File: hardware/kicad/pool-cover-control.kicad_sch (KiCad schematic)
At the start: 20 parts, among them J1 DG128-5.08-04P, Q1 DMP4015SK3Q-13, U1 STM32G031K8Tx, U2 ULN2003A, U3 LMR14206, U4 PC817

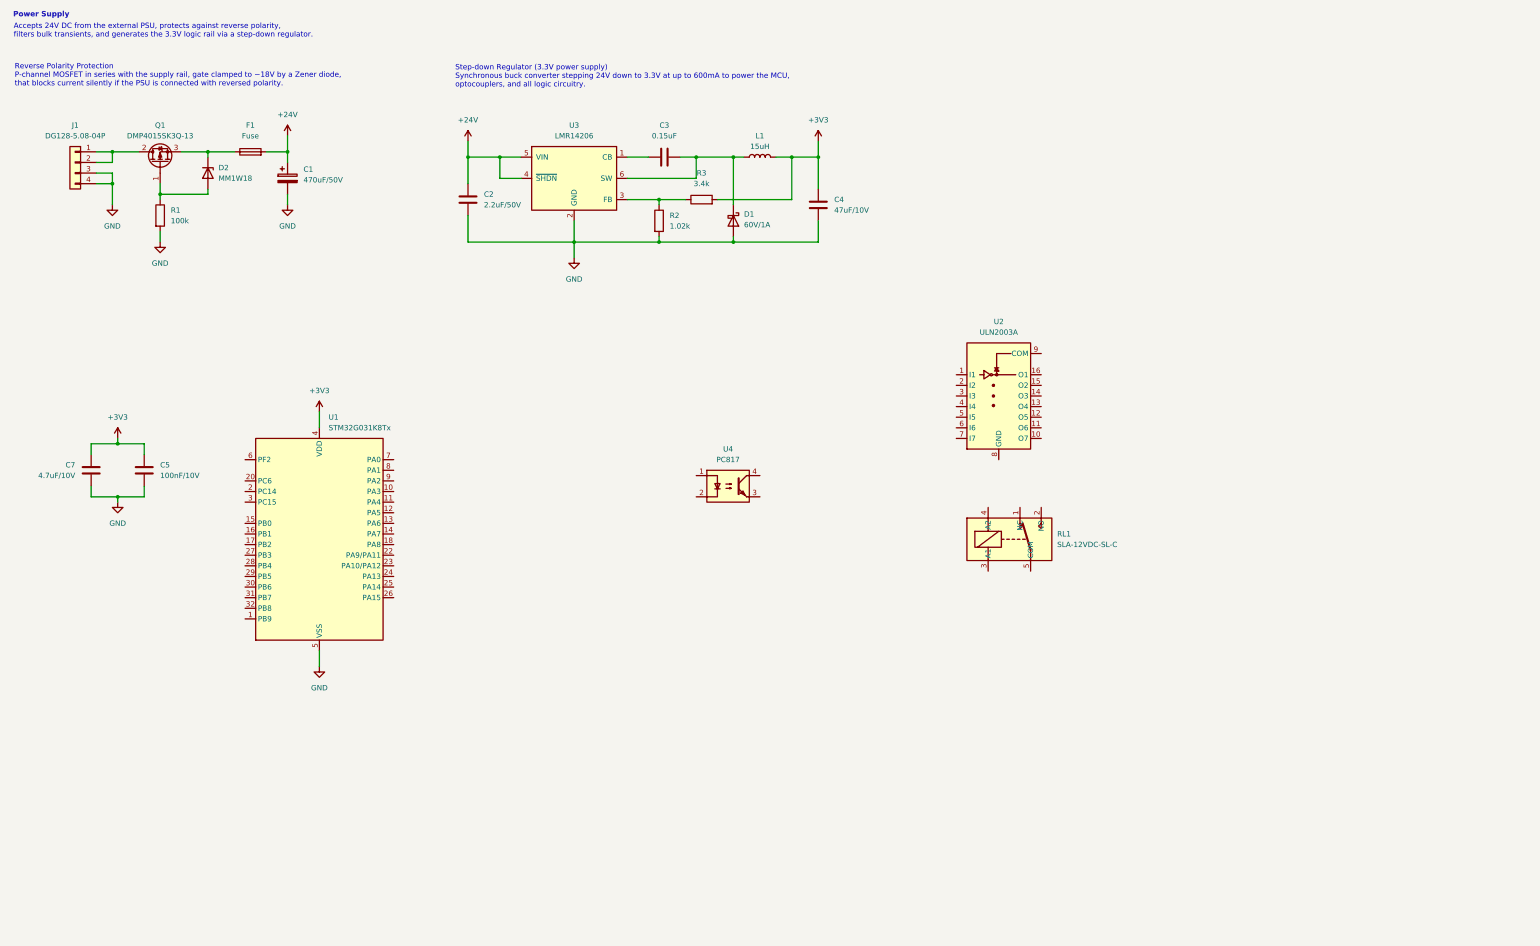
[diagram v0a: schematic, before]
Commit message: feat(hardware): implement SC2 H-bridge schematic
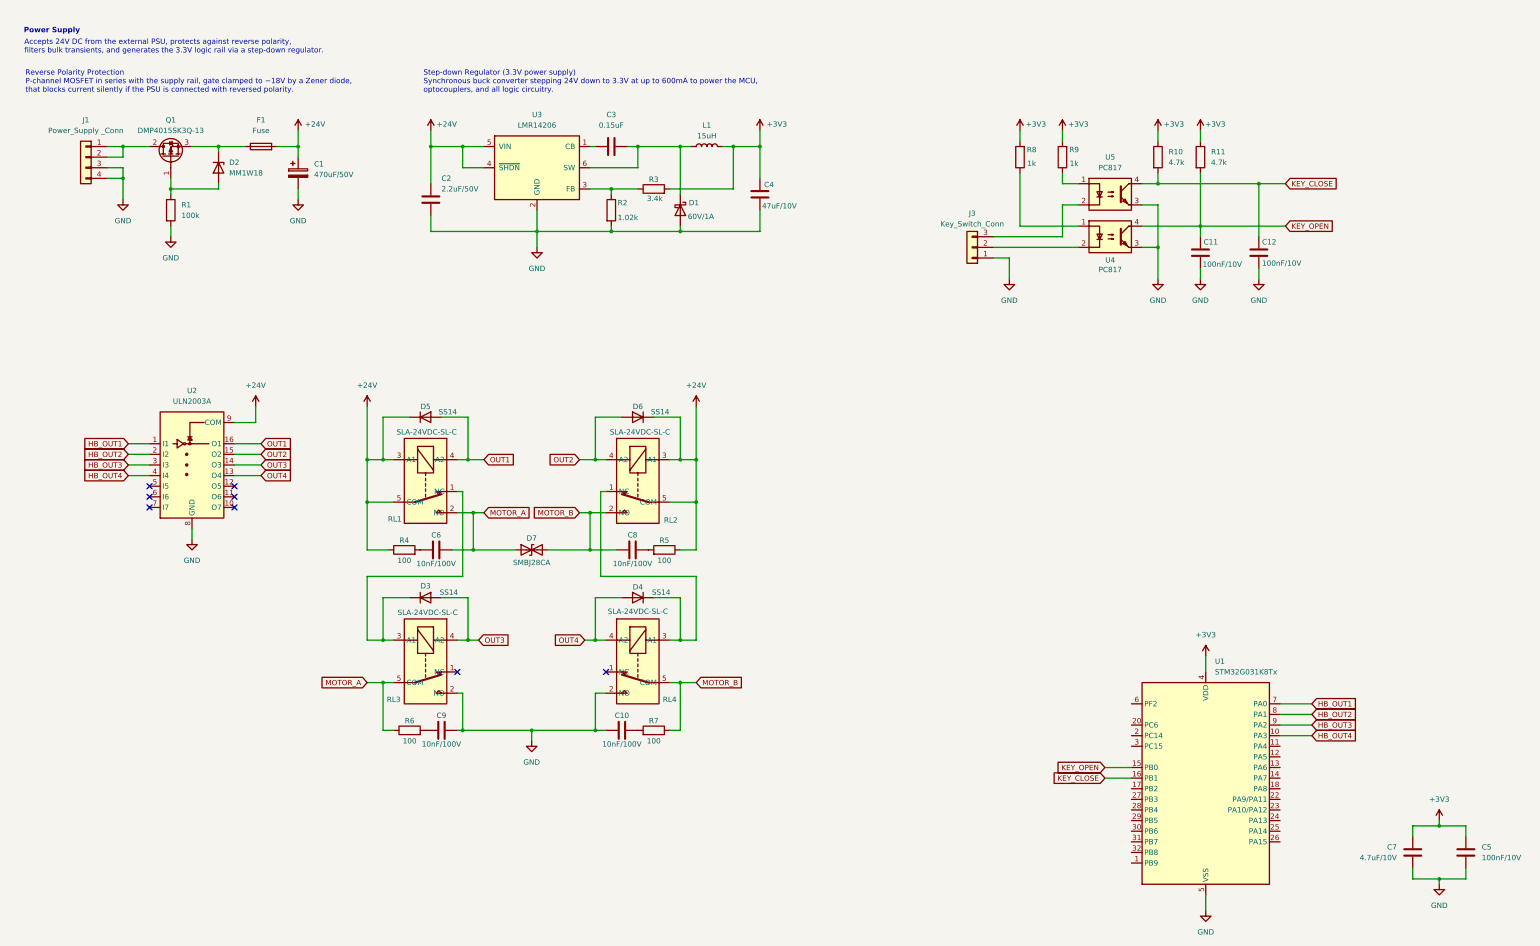
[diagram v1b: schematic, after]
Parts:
- removed RL1: SLA-12VDC-SL-C, pool-cover-control:SLA-12VDC-SL-C, symbol pool-cover-control:SLA-12VDC-SL-C
- added C10, C6, C8, C9: 10nF/100V, Capacitor_SMD:C_0603_1608Metric, symbol Device:C
- added C11, C12: 100nF/10V, Capacitor_SMD:C_0402_1005Metric, symbol Device:C
- added D3, D4, D5, D6: SS14, Diode_SMD:D_SMA, symbol Device:D
- added D7: SMBJ28CA, Diode_SMD:D_SMB, symbol Device:D_TVS
- added J3: Key_Switch_Conn, TerminalBlock_Phoenix:TerminalBlock_Phoenix_MKDS-1,5-3-5.08_1x03_P5.08mm_Horizontal, symbol Connector_Generic:Conn_01x03
- added R10, R11: 4.7k, Resistor_SMD:R_0402_1005Metric, symbol Device:R
- added R4, R5, R6, R7: 100, Resistor_SMD:R_0603_1608Metric, symbol Device:R
- added R8, R9: 1k, Resistor_SMD:R_0402_1005Metric, symbol Device:R
- added RL1, RL2, RL3, RL4: SLA-24VDC-SL-C, pool-cover-control:SLA-24VDC-SL-C, symbol pool-cover-control:SLA-24VDC-SL-C
- added U5: PC817, Package_SO:SOP-4_4.4x2.6mm_P1.27mm, symbol Isolator:PC817
- J1: value DG128-5.08-04P -> Power_Supply _Conn; footprint Connector_Phoenix_MSTB:PhoenixContact_MSTBVA_2,5_4-G-5,08_1x04_P5.08mm_Vertical -> TerminalBlock_Phoenix:TerminalBlock_Phoenix_MKDS-1,5-4-5.08_1x04_P5.08mm_Horizontal; LCSC (none) -> C90087
- U2: footprint (none) -> Package_SO:SOIC-16_3.9x9.9mm_P1.27mm
- U4: LCSC (none) -> C22447129
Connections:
- net +24V: now also U2.9 (COM), D5.1 (K), D6.1 (K), R4.1, R5.1, RL1.3 (A1), RL1.5 (COM), RL2.3 (A1), RL2.5 (COM)
- net +3V3: now also R10.1, R11.1, R8.2, R9.2
- net GND: now also U2.8 (GND), U4.3, C10.2, C11.1, C12.1, C9.2, J3.1 (Pin_1), RL3.2 (NO), RL4.2 (NO), U5.3
- net at U4.1: now also R8.1
- net at U4.2: now also J3.2 (Pin_2)
- net KEY_OPEN: now reaches U4.4
- net KEY_OPEN: now also U1.15 (PB0), C11.2, R11.2
- net HB_OUT1: now reaches U2.1 (I1)
- net HB_OUT1: now also U1.7 (PA0)
- net OUT4: now reaches U2.13 (O4)
- net OUT4: now also D4.2 (A), RL4.4 (A2)
- net OUT3: now reaches U2.14 (O3)
- net OUT3: now also D3.2 (A), RL3.4 (A2)
- net OUT2: now reaches U2.15 (O2)
- net OUT2: now also D6.2 (A), RL2.4 (A2)
- net OUT1: now reaches U2.16 (O1)
- net OUT1: now also D5.2 (A), RL1.4 (A2)
- net HB_OUT2: now reaches U2.2 (I2)
- net HB_OUT2: now also U1.8 (PA1)
- net HB_OUT3: now reaches U2.3 (I3)
- net HB_OUT3: now also U1.9 (PA2)
- net HB_OUT4: now reaches U2.4 (I4)
- net HB_OUT4: now also U1.10 (PA3)
- net KEY_CLOSE: now reaches U1.16 (PB1)
- net KEY_CLOSE: now also C12.2, R10.2, U5.4
- new net: D4.1 (K), RL2.1 (NC), RL4.3 (A1)
- new net: C6.1, R4.2
- new net: D3.1 (K), RL1.1 (NC), RL3.3 (A1)
- new net: C8.1, R5.2
- new net: C9.1, R6.2
- new net: C10.1, R7.2
- new net: J3.3 (Pin_3), U5.2
- new net: R9.1, U5.1
- new net MOTOR_A: C6.2, D7.1 (A1), R6.1, RL1.2 (NO), RL3.5 (COM)
- new net MOTOR_B: C8.2, D7.2 (A2), R7.1, RL2.2 (NO), RL4.5 (COM)
- no-connect marks 0 -> 8
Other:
- moved on the sheet: C1, C2, C3, C4, C5, C7, D1, D2, F1, J1, L1, Q1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

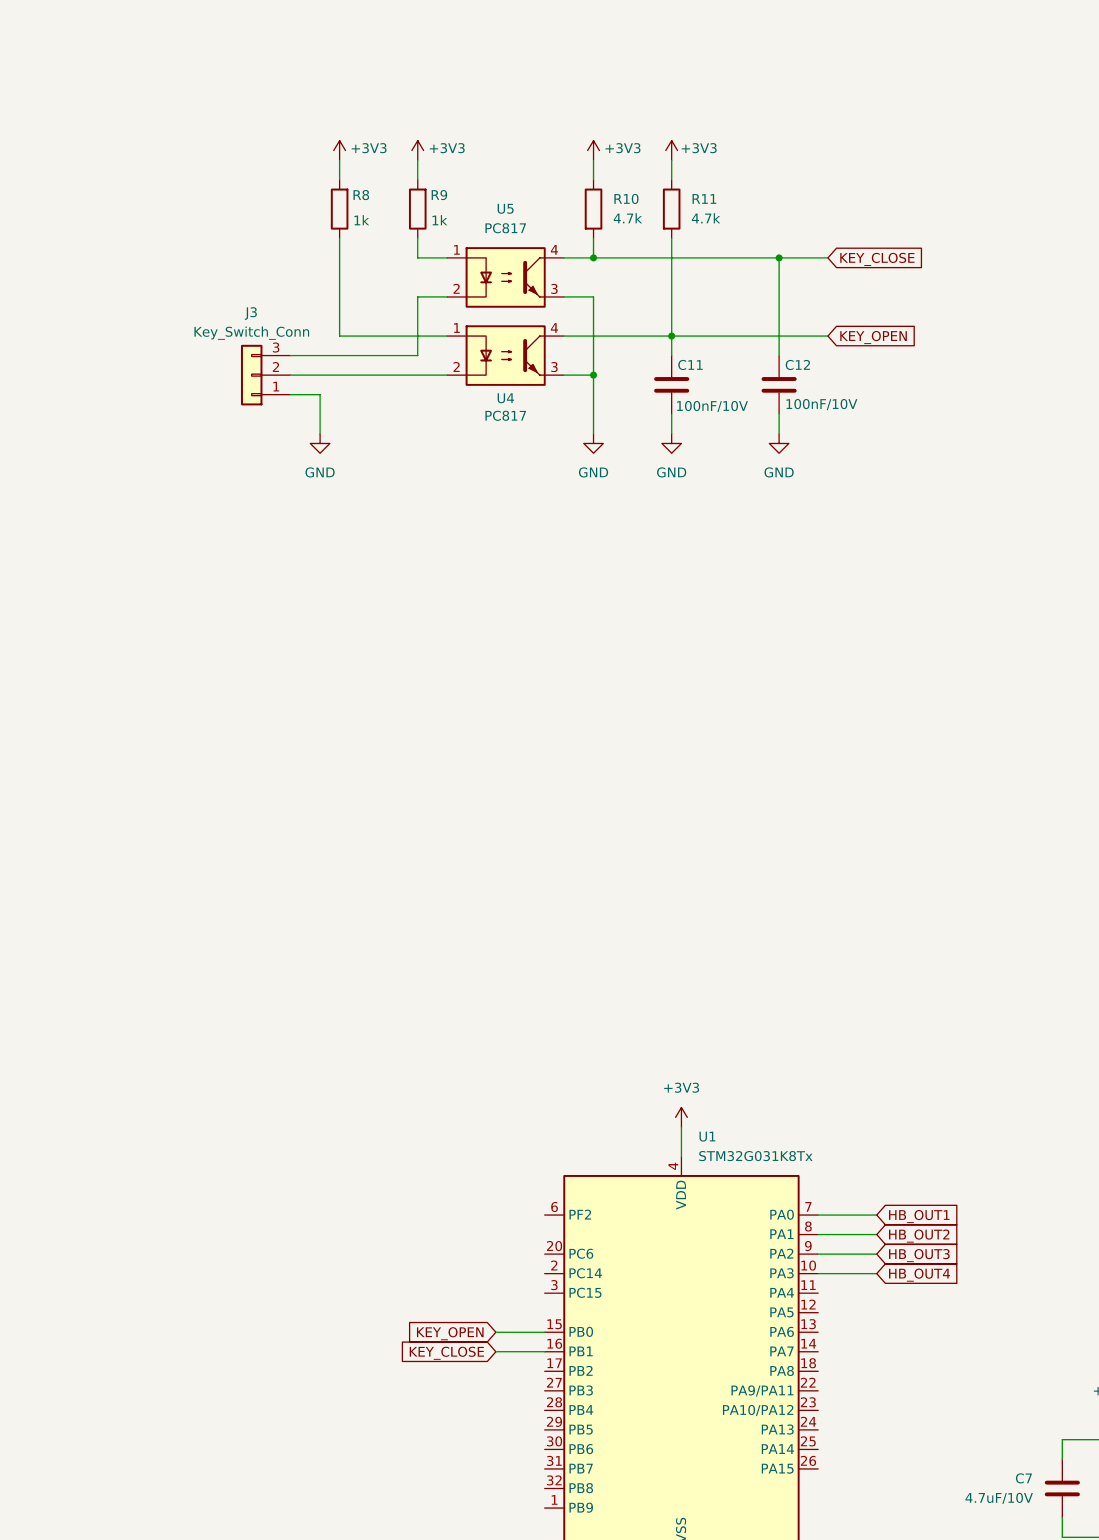
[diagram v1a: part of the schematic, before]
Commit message: feat(hardware): implement SC3 key switch and SC4 limit switch schematic
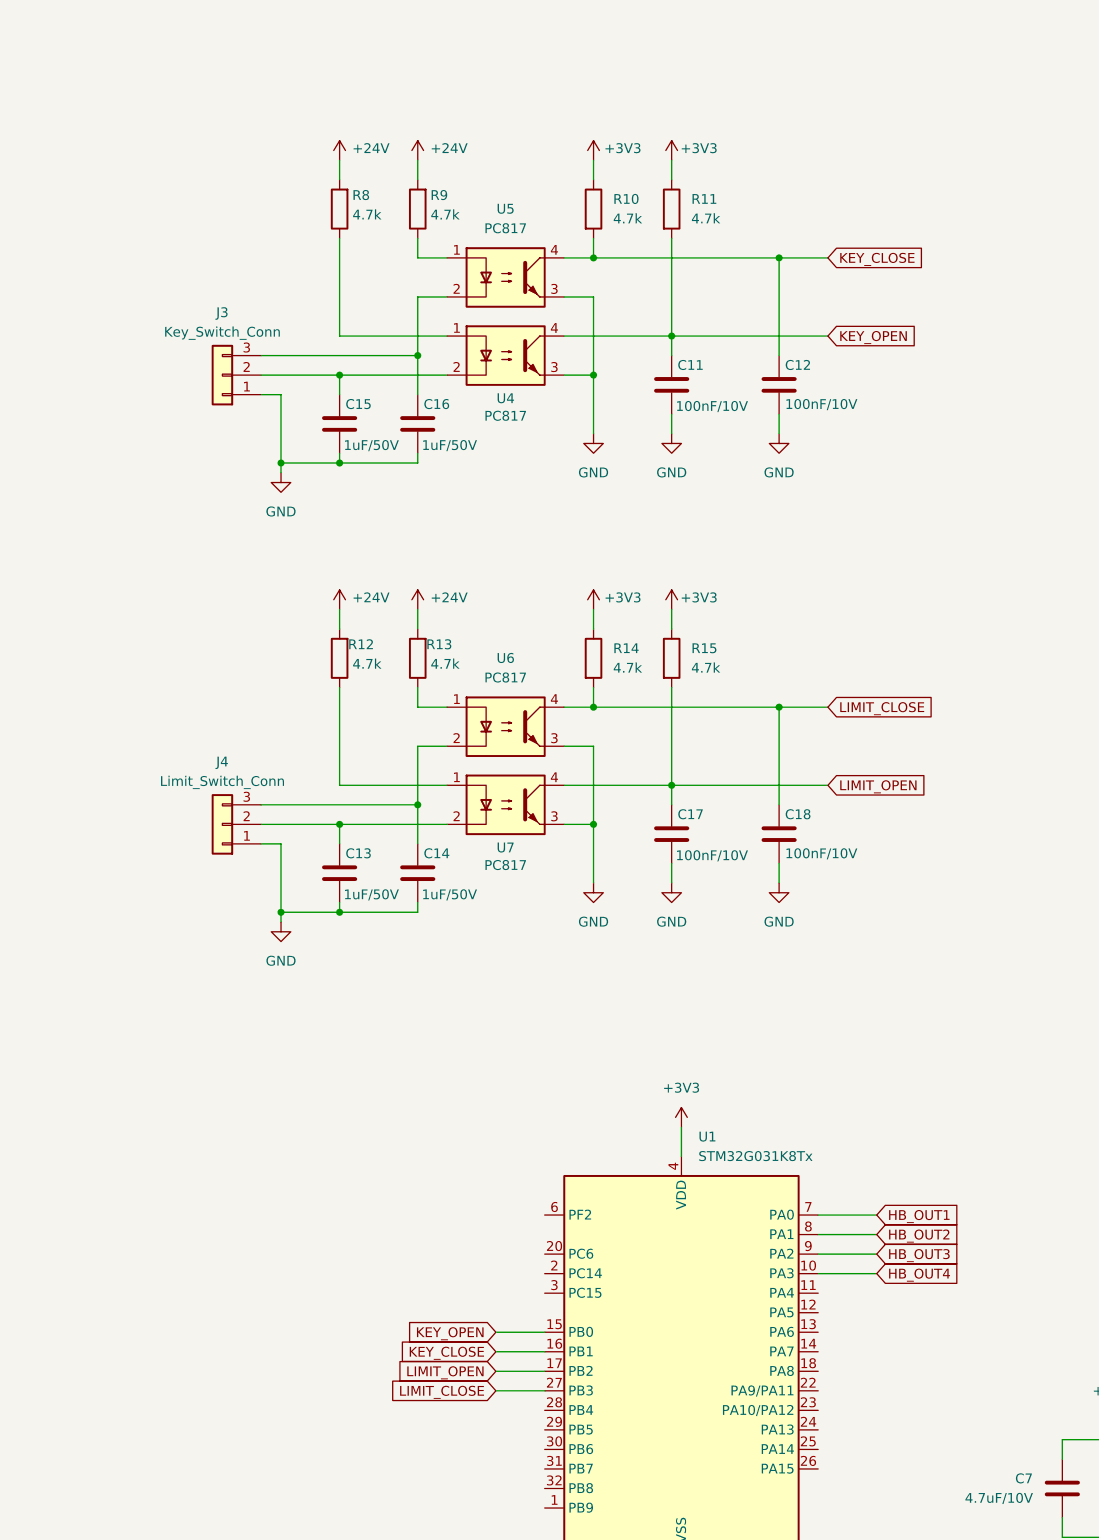
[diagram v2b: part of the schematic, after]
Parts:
- added C13, C14, C15, C16: 1uF/50V, Capacitor_SMD:C_0402_1005Metric, symbol Device:C
- added C17, C18: 100nF/10V, Capacitor_SMD:C_0402_1005Metric, symbol Device:C
- added J4: Limit_Switch_Conn, TerminalBlock_Phoenix:TerminalBlock_Phoenix_MKDS-1,5-3-5.08_1x03_P5.08mm_Horizontal, symbol Connector_Generic:Conn_01x03
- added R12, R13: 4.7k, Resistor_SMD:R_1206_3216Metric_Pad1.30x1.75mm_HandSolder, symbol Device:R
- added R14, R15: 4.7k, Resistor_SMD:R_0402_1005Metric, symbol Device:R
- added U6, U7: PC817, Package_SO:SOP-4_4.4x2.6mm_P1.27mm, symbol Isolator:PC817
- R8, R9: value 1k -> 4.7k; footprint Resistor_SMD:R_0402_1005Metric -> Resistor_SMD:R_1206_3216Metric_Pad1.30x1.75mm_HandSolder
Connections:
- net +24V: now also R8.2, R9.2, R12.2, R13.2
- net +3V3: now also R14.1, R15.1; no longer R8.2, R9.2
- net GND: now also C13.1, C14.1, C15.1, C16.1, C17.1, C18.1, J4.1 (Pin_1), U6.3, U7.3
- net at J3.2 (Pin_2), U4.2: now also C15.2
- net at J3.3 (Pin_3), U5.2: now also C16.2
- net LIMIT_OPEN: now reaches U1.17 (PB2)
- net LIMIT_OPEN: now also C17.2, R15.2, U7.4
- net LIMIT_CLOSE: now reaches U1.27 (PB3)
- net LIMIT_CLOSE: now also C18.2, R14.2, U6.4
- new net: R13.1, U6.1
- new net: C14.2, J4.3 (Pin_3), U6.2
- new net: R12.1, U7.1
- new net: C13.2, J4.2 (Pin_2), U7.2
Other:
- moved on the sheet: J3
